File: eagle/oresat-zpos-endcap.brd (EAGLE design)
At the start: 106 x 106 mm, 28 parts, among them U1 TCA9543A-PW, U3 HMC5883L, U4 HMC5883L

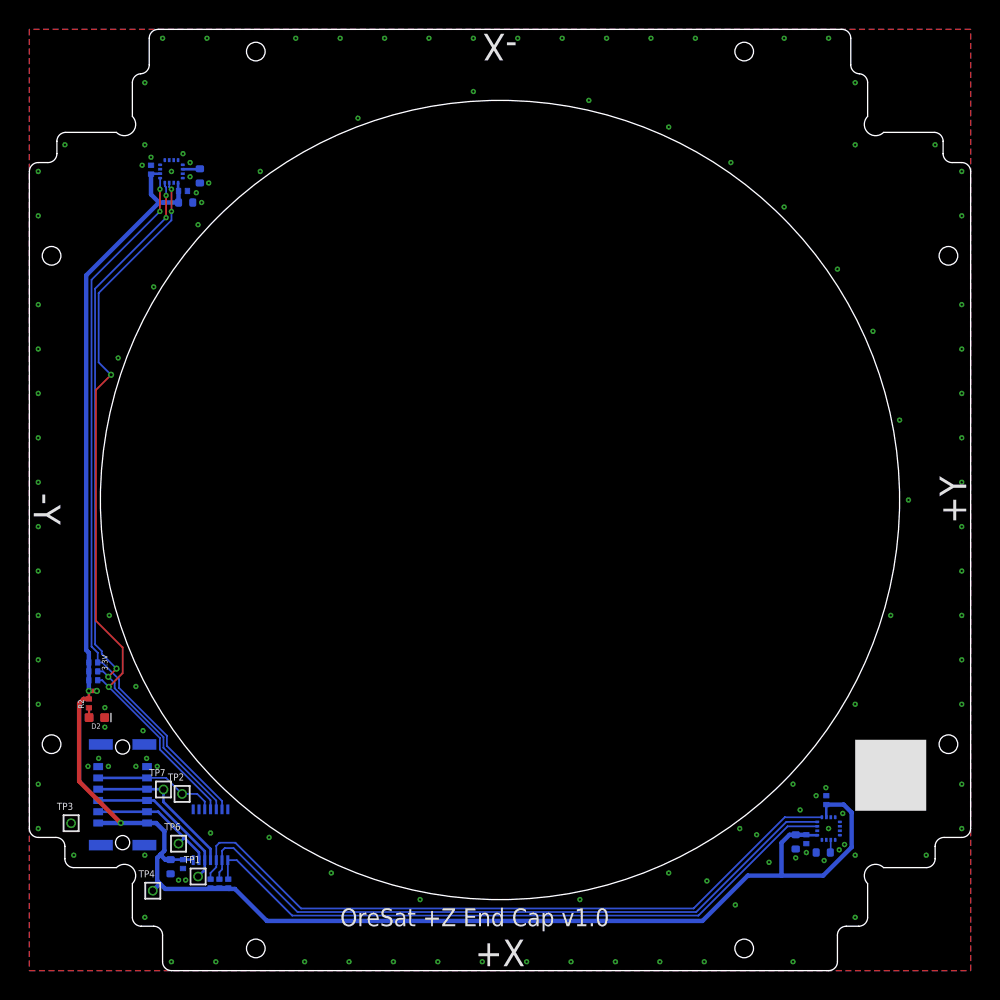
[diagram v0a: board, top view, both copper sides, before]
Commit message: Updated outline based on new symmetrical end caps, decreased hole size but kept ground plane back.
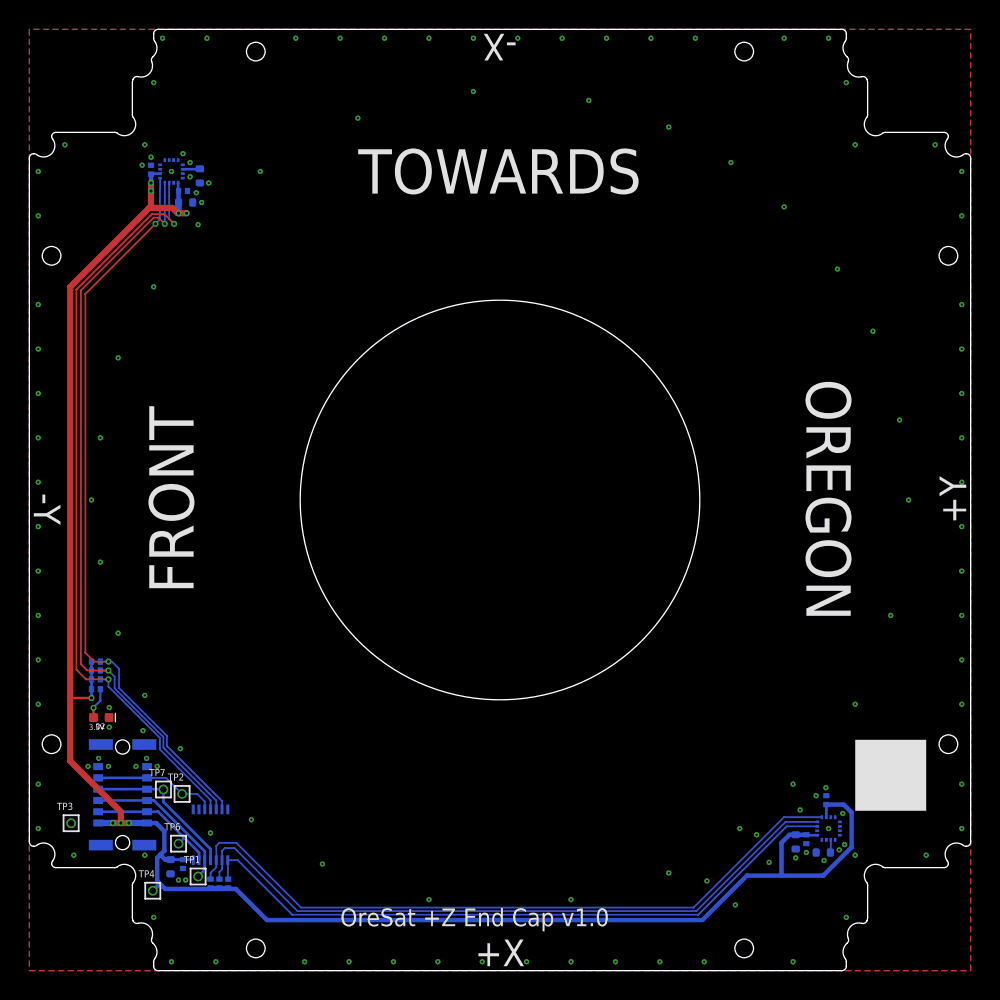
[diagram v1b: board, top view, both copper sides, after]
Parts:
- moved R2 1.79 mm to (7.50, 31.7), flipped to the bottom, turned to 0 degrees
- moved D2 0.50 mm to (8.10, 28.5)
- moved R1 0.32 mm to (7.50, 32.8)
- moved R4 0.32 mm to (7.50, 34.8)
- moved R5 0.32 mm to (7.50, 33.8)
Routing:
- net 3.3V: track 208.2 -> 218.4 mm, vias 3 -> 8
- net !INT0: track 83.5 -> 87.0 mm, vias 4 -> 2
- net SDA0: track 81.8 -> 84.8 mm, vias 4 -> 2
- net N$271: track 1.12 -> 3.52 mm, vias 0 -> 1
- net SCL0: track 80.7 -> 83.0 mm
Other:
- outline, holes or cut-outs redrawn
- board text added: "FRONT"
- board text added: "OREGON"
- board text added: "TOWARDS"
